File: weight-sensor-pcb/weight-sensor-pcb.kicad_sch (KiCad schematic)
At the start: 0 parts

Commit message: attempt at force sensor & analog front end schematic
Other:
- added sheet CAN Interface (can_interface.kicad_sch)
- added sheet Force Sensor & Analog Front-End (force_sensor_analog_fe.kicad_sch)
- added sheet Power Supply (power_supply.kicad_sch)
- added sheet STM32 Microcontroller (stm32_mcu.kicad_sch)
- title: (none) -> Force Sensor CAN Interface Board
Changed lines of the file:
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@@
 	(generator_version "9.0")
 	(paper "A4")
+	(title_block
+		(title "Force Sensor CAN Interface Board")
+	)
+	(sheet
+		(at 39.37 57.785)
+		(size 12.7 3.81)
+		(exclude_from_sim no)
+		(in_bom yes)
+		(on_board yes)
+		(dnp no)
+		(fields_autoplaced yes)
+		(stroke
+			(width 0.1524)
+			(type solid)
+		)
+		(fill
+			(color 0 0 0 0.0000)
+		)
+		(property "Sheetname" "CAN Interface"
+			(at 39.37 57.0734 0)
+			(effects
+				(font
+					(size 1.27 1.27)
+				)
+				(justify left bottom)
+			)
+		)
+		(property "Sheetfile" "can_interface.kicad_sch"
+			(at 39.37 62.1796 0)
+			(effects
+				(font
+					(size 1.27 1.27)
+				)
+				(justify left top)
+			)
+		)
+		(instances
+			(project "weight-sensor-pcb"
+				(path "/030ca1f5-68f0-4323-9a91-656d7965b13e"
+					(page "5")
+				)
+			)
+		)
+	)
+	(sheet
+		(at 85.09 40.64)
+		(size 12.7 3.81)
+		(exclude_from_sim no)
+		(in_bom yes)
+		(on_board yes)
+		(dnp no)
+		(fields_autoplaced yes)
+		(stroke
+			(width 0.1524)
+			(type solid)
+		)
+		(fill
+			(color 0 0 0 0.0000)
+		)
+		(property "Sheetname" "Force Sensor & Analog Front-End"
+			(at 85.09 39.9284 0)
+			(effects
+				(font
+					(size 1.27 1.27)
+				)
+				(justify left bottom)
+			)
+		)
+		(property "Sheetfile" "force_sensor_analog_fe.kicad_sch"
+			(at 85.09 45.0346 0)
+			(effects
+				(font
+					(size 1.27 1.27)
+				)
+				(justify left top)
+			)
+		)
+		(instances
+			(project "weight-sensor-pcb"
+				(path "/030ca1f5-68f0-4323-9a91-656d7965b13e"
+					(page "2")
+				)
+			)
+		)
+	)
+	(sheet
+		(at 39.37 40.64)
+		(size 12.7 3.81)
+		(exclude_from_sim no)
+		(in_bom yes)
+		(on_board yes)
+		(dnp no)
+		(fields_autoplaced yes)
+		(stroke
+			(width 0.1524)
+			(type solid)
+		)
+		(fill
+			(color 0 0 0 0.0000)
+		)
+		(property "Sheetname" "Power Supply"
+			(at 39.37 39.9284 0)
+			(effects
+				(font
+					(size 1.27 1.27)
+				)
+				(justify left bottom)
+			)
+		)
+		(property "Sheetfile" "power_supply.kicad_sch"
+			(at 39.37 45.0346 0)
+			(effects
+				(font
+					(size 1.27 1.27)
+				)
+				(justify left top)
+			)
+		)
+		(instances
+			(project "weight-sensor-pcb"
+				(path "/030ca1f5-68f0-4323-9a91-656d7965b13e"
+					(page "4")
+				)
+			)
+		)
+	)
+	(sheet
+		(at 133.35 40.64)
+		(size 12.7 3.81)
+		(exclude_from_sim no)
+		(in_bom yes)
+		(on_board yes)
+		(dnp no)
+		(fields_autoplaced yes)
+		(stroke
+			(width 0.1524)
+			(type solid)
+		)
+		(fill
+			(color 0 0 0 0.0000)
+		)
+		(property "Sheetname" "STM32 Microcontroller"
+			(at 133.35 39.9284 0)
+			(effects
+				(font
+					(size 1.27 1.27)
+				)
+				(justify left bottom)
+			)
+		)
+		(property "Sheetfile" "stm32_mcu.kicad_sch"
+			(at 133.35 45.0346 0)
+			(effects
+				(font
+					(size 1.27 1.27)
+				)
+				(justify left top)
+			)
+		)
+		(instances
+			(project "weight-sensor-pcb"
+				(path "/030ca1f5-68f0-4323-9a91-656d7965b13e"
+					(page "3")
+				)
+			)
+		)
+	)
 	(sheet_instances
 		(path "/"

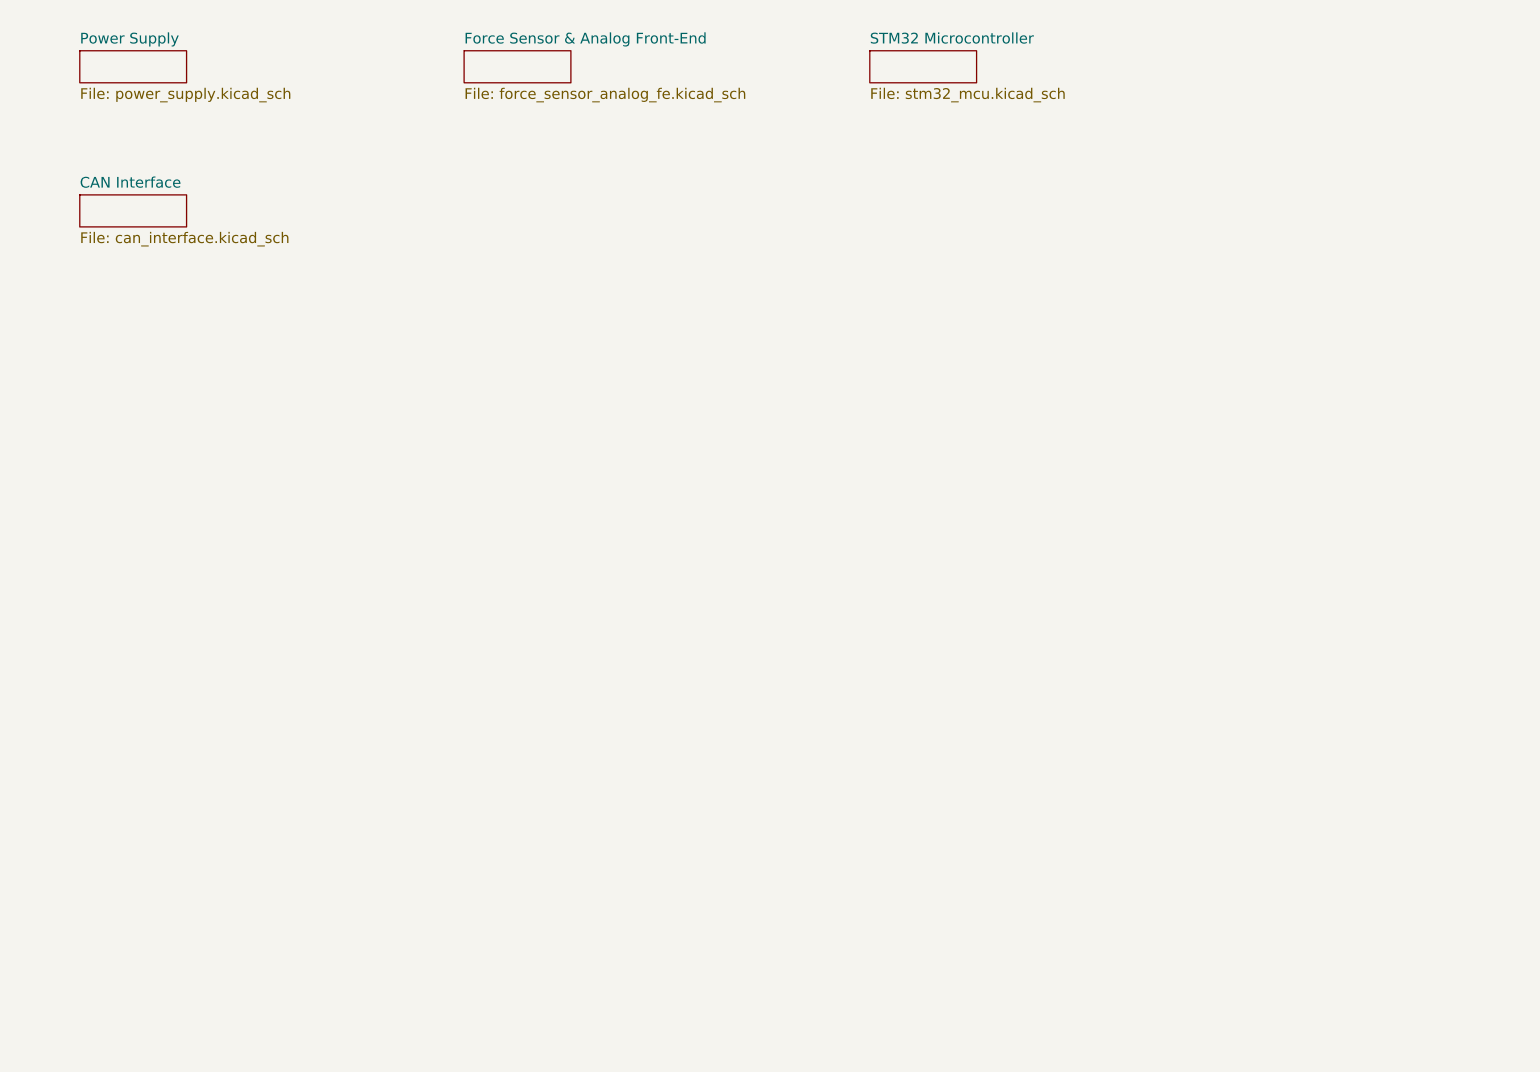
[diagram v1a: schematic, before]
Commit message: Add hierarchial labels to MCU and CAN Interface sheets
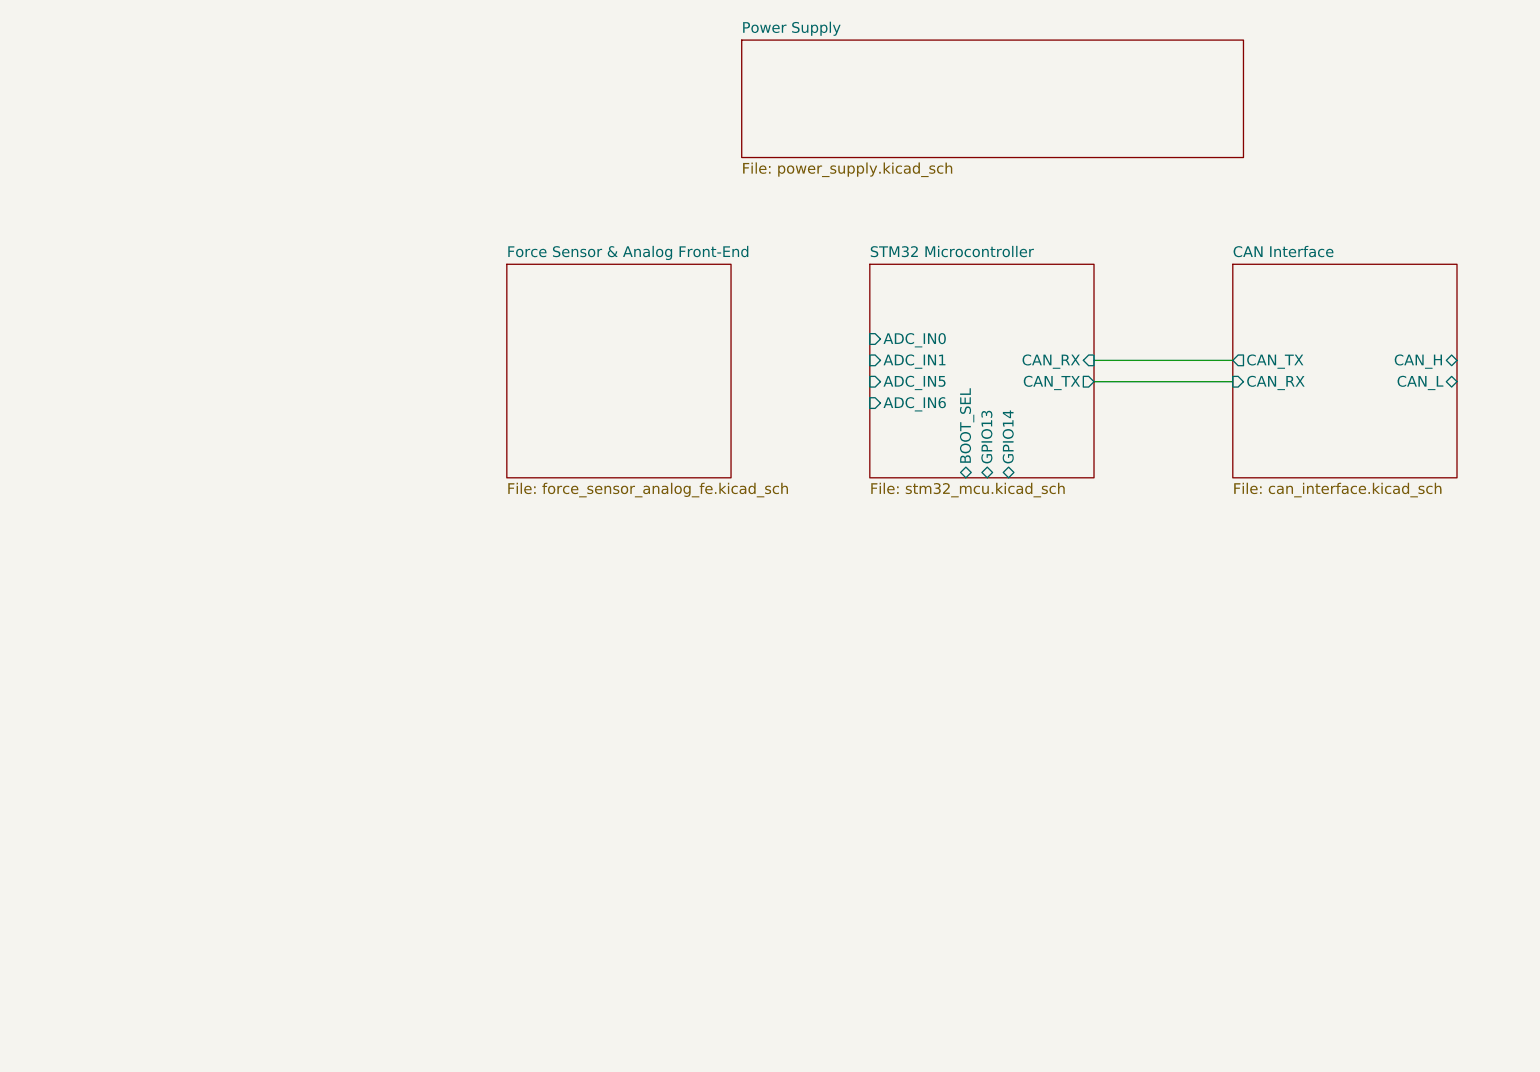
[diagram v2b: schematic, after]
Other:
- sheet CAN Interface ports: added CAN_H, CAN_L, CAN_RX, CAN_TX; removed none
- sheet STM32 Microcontroller ports: added ADC_IN0, ADC_IN1, ADC_IN5, ADC_IN6, BOOT_SEL, CAN_RX, CAN_TX, GPIO13, GPIO14; removed none
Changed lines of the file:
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@@
 		(title "Force Sensor CAN Interface Board")
 	)
-	(sheet
-		(at 39.37 57.785)
-		(size 12.7 3.81)
+	(wire
+		(pts
+			(xy 160.02 77.47) (xy 176.53 77.47)
+		)
+		(stroke
+			(width 0)
+			(type default)
+		)
+	)
+	(wire
+		(pts
+			(xy 160.02 80.01) (xy 176.53 80.01)
+		)
+		(stroke
+			(width 0)
+			(type default)
+		)
+	)
+	(sheet
+		(at 176.53 66.04)
+		(size 26.67 25.4)
 		(exclude_from_sim no)
 		(in_bom yes)
@@
 		)
 		(property "Sheetname" "CAN Interface"
-			(at 39.37 57.0734 0)
+			(at 176.53 65.3284 0)
 			(effects
 				(font
@@
 		)
 		(property "Sheetfile" "can_interface.kicad_sch"
-			(at 39.37 62.1796 0)
-			(effects
-				(font
-					(size 1.27 1.27)
-				)
-				(justify left top)
+			(at 176.53 92.0246 0)
+			(effects
+				(font
+					(size 1.27 1.27)
+				)
+				(justify left top)
+			)
+		)
+		(pin "CAN_TX" output
+			(at 176.53 77.47 180)
+			(effects
+				(font
+					(size 1.27 1.27)
+				)
+				(justify left)
+			)
+		)
+		(pin "CAN_RX" input
+			(at 176.53 80.01 180)
+			(effects
+				(font
+					(size 1.27 1.27)
+				)
+				(justify left)
+			)
+		)
+		(pin "CAN_L" bidirectional
+			(at 203.2 80.01 0)
+			(effects
+				(font
+					(size 1.27 1.27)
+				)
+				(justify right)
+			)
+		)
+		(pin "CAN_H" bidirectional
+			(at 203.2 77.47 0)
+			(effects
+				(font
+					(size 1.27 1.27)
+				)
+				(justify right)
 			)
 		)
@@
 	)
 	(sheet
-		(at 85.09 40.64)
-		(size 12.7 3.81)
+		(at 90.17 66.04)
+		(size 26.67 25.4)
 		(exclude_from_sim no)
 		(in_bom yes)
@@
 		)
 		(property "Sheetname" "Force Sensor & Analog Front-End"
-			(at 85.09 39.9284 0)
+			(at 90.17 65.3284 0)
 			(effects
 				(font
@@
 		)
 		(property "Sheetfile" "force_sensor_analog_fe.kicad_sch"
-			(at 85.09 45.0346 0)
+			(at 90.17 92.0246 0)
 			(effects
 				(font
@@
 	)
 	(sheet
-		(at 39.37 40.64)
-		(size 12.7 3.81)
+		(at 118.11 39.37)
+		(size 59.69 13.97)
 		(exclude_from_sim no)
 		(in_bom yes)
@@
 		)
 		(property "Sheetname" "Power Supply"
-			(at 39.37 39.9284 0)
+			(at 118.11 38.6584 0)
 			(effects
 				(font
@@
 		)
 		(property "Sheetfile" "power_supply.kicad_sch"
-			(at 39.37 45.0346 0)
+			(at 118.11 53.9246 0)
 			(effects
 				(font
@@
 	)
 	(sheet
-		(at 133.35 40.64)
-		(size 12.7 3.81)
+		(at 133.35 66.04)
+		(size 26.67 25.4)
 		(exclude_from_sim no)
 		(in_bom yes)
@@
 		)
 		(property "Sheetname" "STM32 Microcontroller"
-			(at 133.35 39.9284 0)
+			(at 133.35 65.3284 0)
 			(effects
 				(font
@@
 		)
 		(property "Sheetfile" "stm32_mcu.kicad_sch"
-			(at 133.35 45.0346 0)
-			(effects
-				(font
-					(size 1.27 1.27)
-				)
-				(justify left top)
-			)
-		)
+			(at 133.35 92.0246 0)
+			(effects
+				(font
+					(size 1.27 1.27)
+				)
+				(justify left top)
+			)
+		)
+		(pin "ADC_IN0" input
+			(at 133.35 74.93 180)
+			(effects
+				(font
+					(size 1.27 1.27)
+				)
+				(justify left)
+			)
+		)
+		(pin "ADC_IN1" input
+			(at 133.35 77.47 180)
+			(effects
+				(font
+					(size 1.27 1.27)
+				)
+				(justify left)
+			)
+		)
+		(pin "ADC_IN6" input
+			(at 133.35 82.55 180)
+			(effects
+				(font
+					(size 1.27 1.27)
+				)
+				(justify left)
+			)
+		)
+		(pin "ADC_IN5" input
+			(at 133.35 80.01 180)
+			(effects
+				(font
+					(size 1.27 1.27)
+				)
+				(justify left)
+			)
+		)
+		(pin "CAN_TX" output
+			(at 160.02 80.01 0)
+			(effects
+				(font
+					(size 1.27 1.27)
+				)
+				(justify right)
+			)
+		)
+		(pin "CAN_RX" input
+			(at 160.02 77.47 0)
+			(effects
+				(font
+					(size 1.27 1.27)
+				)
+				(justify right)
+			)
+		)
+		(pin "GPIO13" bidirectional
+			(at 147.32 91.44 270)
+			(effects
+				(font
+					(size 1.27 1.27)
+				)
+				(justify left)
+			)
+		)
+		(pin "BOOT_SEL" bidirectional
+			(at 144.78 91.44 270)
+			(effects
+				(font
+					(size 1.27 1.27)
+				)
+				(justify left)
+			)
+		)
+		(pin "GPIO14" bidirectional
+			(at 149.86 91.44 270)
+			(effects
+				(font
+					(size 1.27 1.27)
+				)
+				(justify left)
+			)
+		)

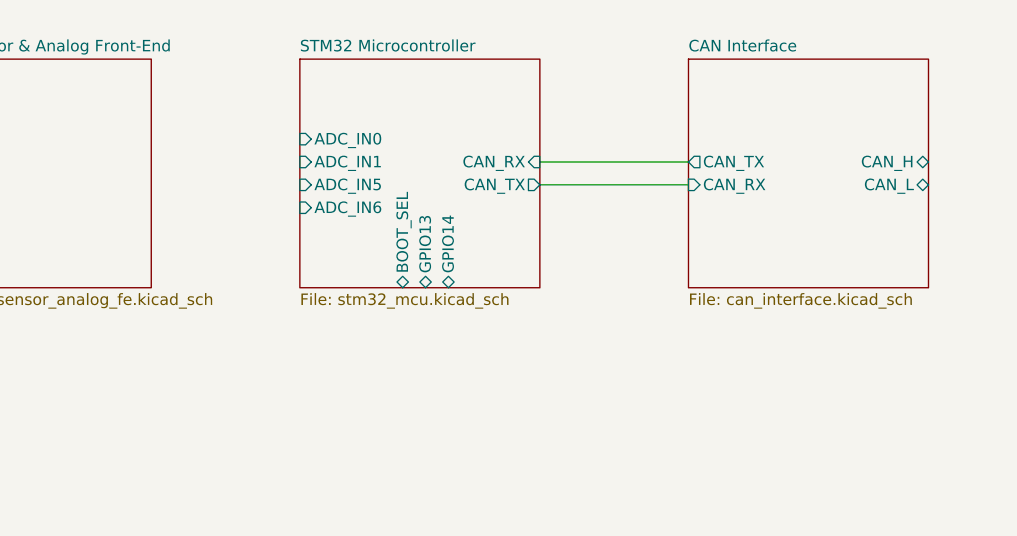
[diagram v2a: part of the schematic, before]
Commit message: Add Test points, CAN connector, USART connector
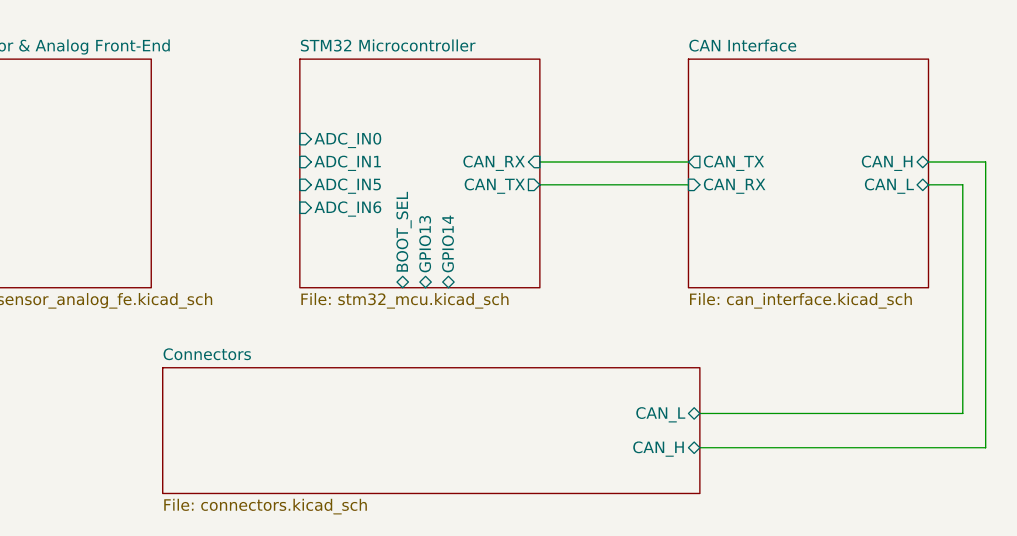
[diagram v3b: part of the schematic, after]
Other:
- added sheet Connectors (connectors.kicad_sch)
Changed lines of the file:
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@@
+	(wire
+		(pts
+			(xy 209.55 77.47) (xy 209.55 109.22)
+		)
+		(stroke
+			(width 0)
+			(type default)
+		)
+	)
+	(wire
+		(pts
+			(xy 177.8 105.41) (xy 207.01 105.41)
+		)
+		(stroke
+			(width 0)
+			(type default)
+		)
+	)
+	(wire
+		(pts
+			(xy 207.01 80.01) (xy 203.2 80.01)
+		)
+		(stroke
+			(width 0)
+			(type default)
+		)
+	)
+	(wire
+		(pts
+			(xy 177.8 109.22) (xy 209.55 109.22)
+		)
+		(stroke
+			(width 0)
+			(type default)
+		)
+	)
 	(wire
 		(pts
 			(xy 160.02 77.47) (xy 176.53 77.47)
+		)
+		(stroke
+			(width 0)
+			(type default)
+		)
+	)
+	(wire
+		(pts
+			(xy 207.01 105.41) (xy 207.01 80.01)
+		)
+		(stroke
+			(width 0)
+			(type default)
+		)
+	)
+	(wire
+		(pts
+			(xy 203.2 77.47) (xy 209.55 77.47)
 		)
 		(stroke
@@
 				)
 			)
+		)
+	)
+	(sheet
+		(at 118.1099 100.3299)
+		(size 59.69 13.97)
+		(exclude_from_sim no)
+		(in_bom yes)
+		(on_board yes)
+		(dnp no)
+		(fields_autoplaced yes)
+		(stroke
+			(width 0.1524)
+			(type solid)
+		)
+		(fill
+			(color 0 0 0 0.0000)
+		)
+		(property "Sheetname" "Connectors"
+			(at 118.1099 99.6183 0)
+			(effects
+				(font
+					(size 1.27 1.27)
+				)
+				(justify left bottom)
+			)
+		)
+		(property "Sheetfile" "connectors.kicad_sch"
+			(at 118.1099 114.8845 0)
+			(effects
+				(font
+					(size 1.27 1.27)
+				)
+				(justify left top)
+			)
+		)
+		(pin "CAN_H" bidirectional
+			(at 177.7999 109.22 0)
+			(effects
+				(font
+					(size 1.27 1.27)
+				)
+				(justify right)
+			)
+		)
+		(pin "CAN_L" bidirectional
+			(at 177.7999 105.41 0)
+			(effects
+				(font
+					(size 1.27 1.27)
+				)
+				(justify right)
+			)
+		)
+		(instances
+			(project "weight-sensor-pcb"
+				(path "/030ca1f5-68f0-4323-9a91-656d7965b13e"
+					(page "6")
+				)
+			)

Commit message: layout progress 1
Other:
- sheet Force Sensor & Analog Front-End ports: added S1, S2, S3, S4; removed none
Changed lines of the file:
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@@
+	(wire
+		(pts
+			(xy 116.84 77.47) (xy 133.35 77.47)
+		)
+		(stroke
+			(width 0)
+			(type default)
+		)
+	)
+	(wire
+		(pts
+			(xy 116.84 74.93) (xy 133.35 74.93)
+		)
+		(stroke
+			(width 0)
+			(type default)
+		)
+	)
+	(wire
+		(pts
+			(xy 116.84 80.01) (xy 133.35 80.01)
+		)
+		(stroke
+			(width 0)
+			(type default)
+		)
+	)
 	(wire
 		(pts
@@
 		(pts
 			(xy 160.02 77.47) (xy 176.53 77.47)
+		)
+		(stroke
+			(width 0)
+			(type default)
+		)
+	)
+	(wire
+		(pts
+			(xy 116.84 82.55) (xy 133.35 82.55)
 		)
 		(stroke
@@
 			)
 		)
+		(pin "S1" output
+			(at 116.84 74.93 0)
+			(effects
+				(font
+					(size 1.27 1.27)
+				)
+				(justify right)
+			)
+		)
+		(pin "S2" output
+			(at 116.84 77.47 0)
+			(effects
+				(font
+					(size 1.27 1.27)
+				)
+				(justify right)
+			)
+		)
+		(pin "S3" output
+			(at 116.84 80.01 0)
+			(effects
+				(font
+					(size 1.27 1.27)
+				)
+				(justify right)
+			)
+		)
+		(pin "S4" output
+			(at 116.84 82.55 0)
+			(effects
+				(font
+					(size 1.27 1.27)
+				)
+				(justify right)
+			)
+		)

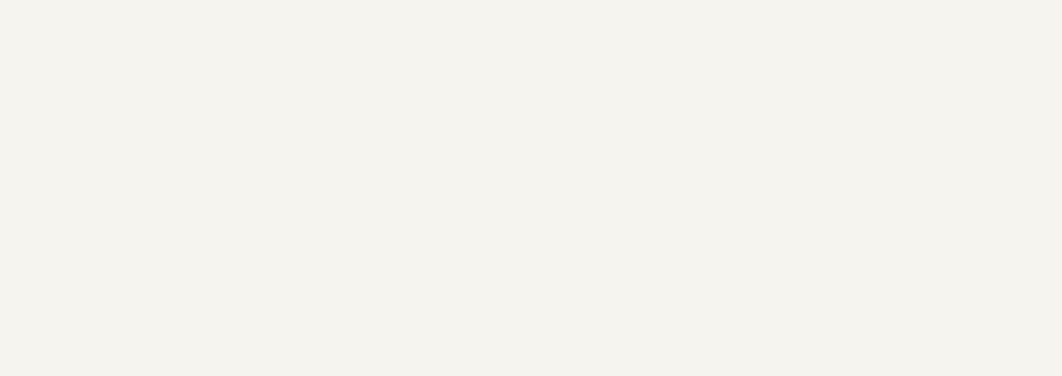
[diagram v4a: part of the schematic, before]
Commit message: more layout updates, add mounting hole pads to schematic
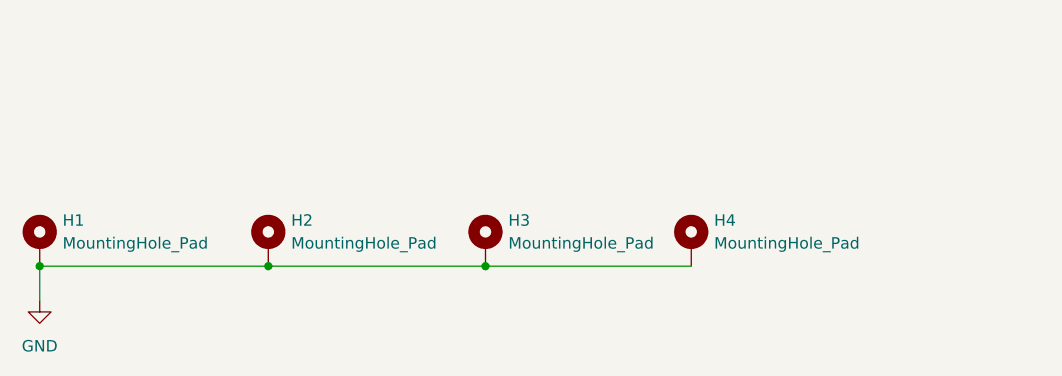
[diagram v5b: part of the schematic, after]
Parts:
- added H1, H2, H3, H4: MountingHole_Pad, MountingHole:MountingHole_2.2mm_M2_Pad_Via, symbol Mechanical:MountingHole_Pad
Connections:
- new net GND: H1.1, H2.1, H3.1, H4.1
